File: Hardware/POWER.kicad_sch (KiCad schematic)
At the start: 57 parts, among them J4 Conn_01x02, U3 TLV62080DSGR, U4 RT7272BGSP, U5 TPS259260DRCR

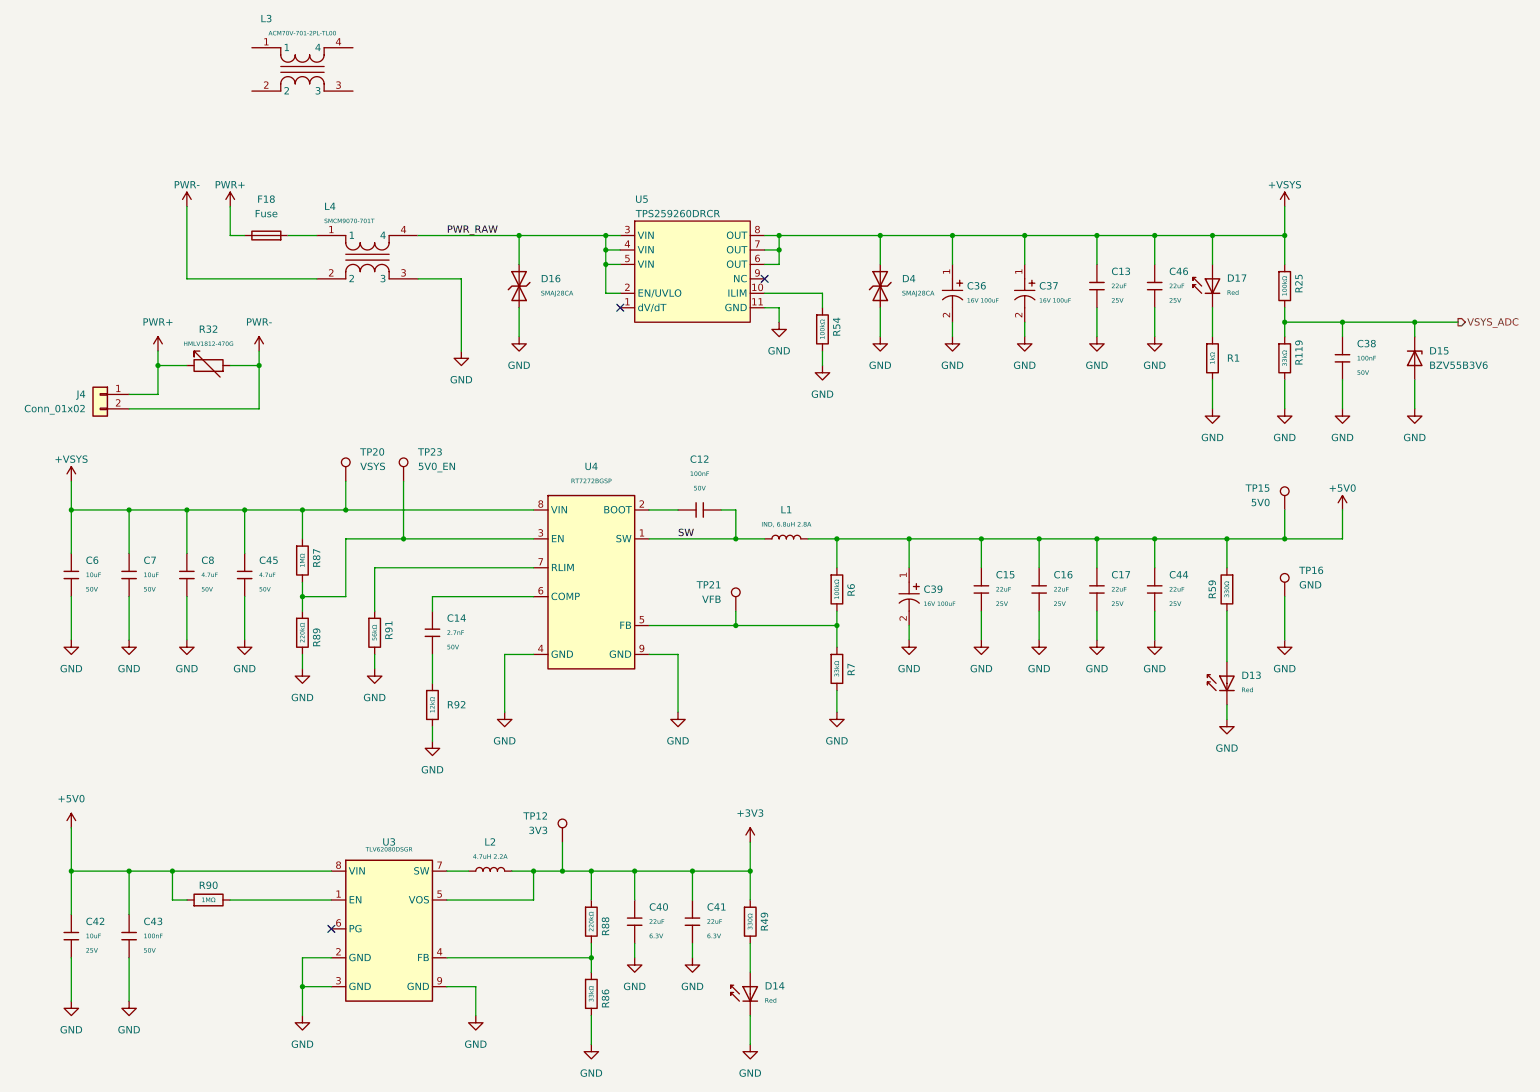
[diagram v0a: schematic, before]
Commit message: remove unused sheets
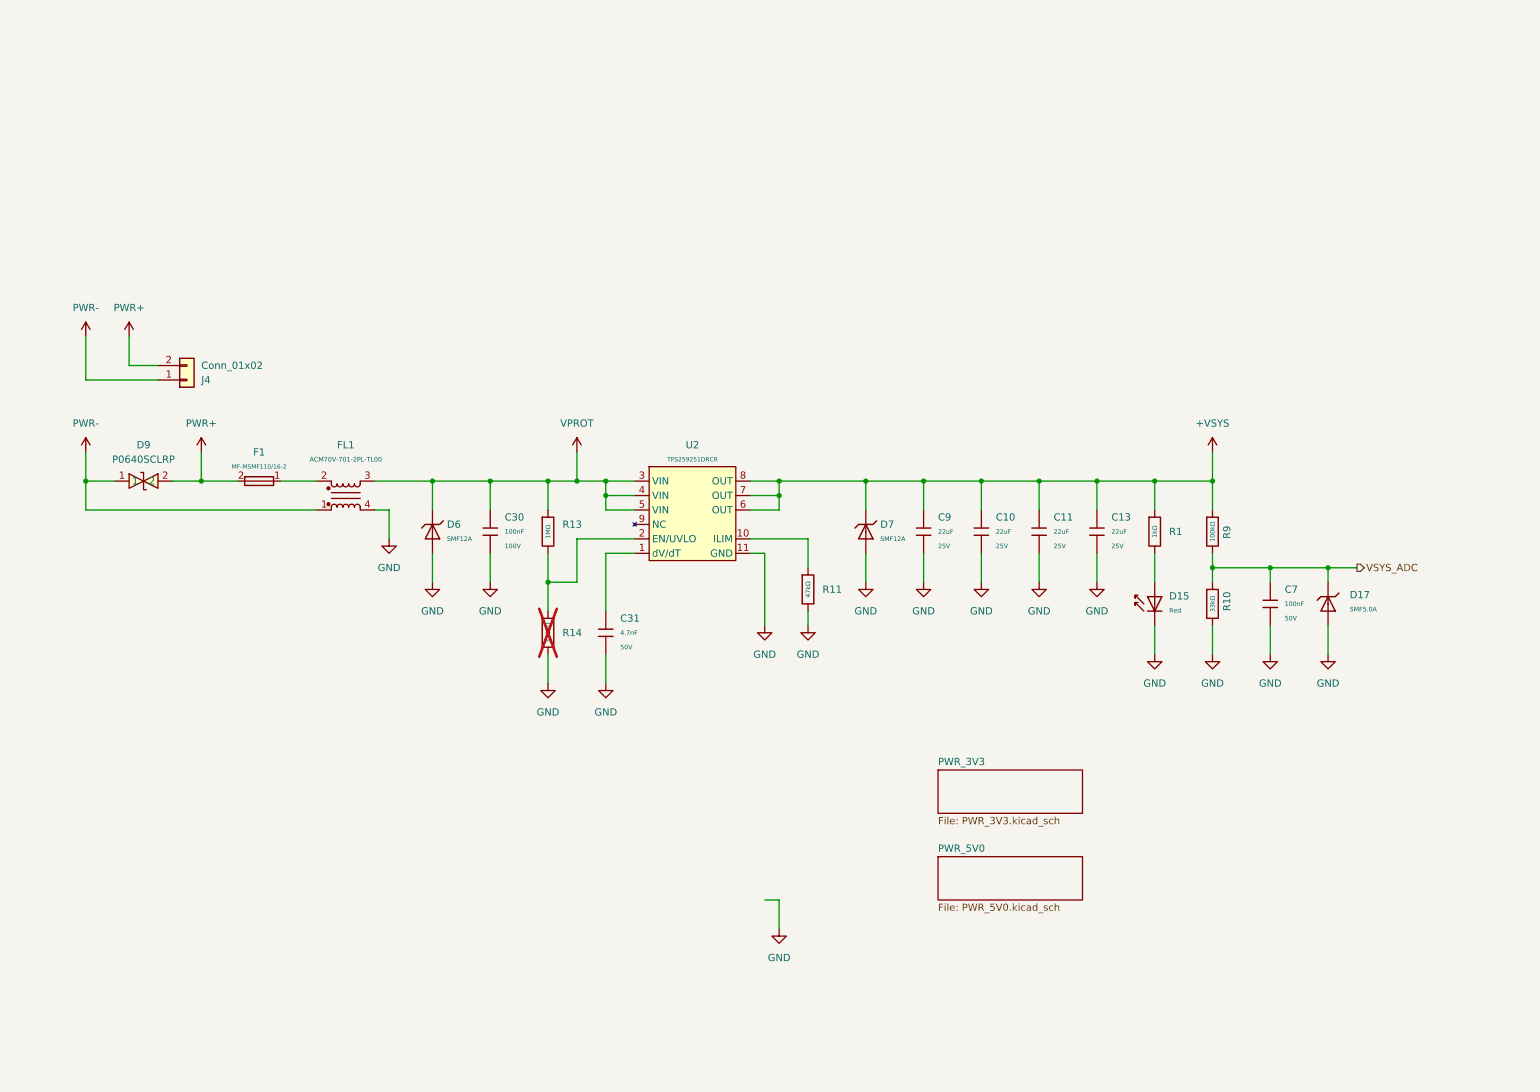
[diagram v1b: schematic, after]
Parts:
- removed C12, C38, C43: 100nF, PCM_JLCPCB:C_0603, symbol PCM_JLCPCB-Capacitors:0603,100nF
- removed C14: 2.7nF, PCM_JLCPCB:C_0603, symbol PCM_JLCPCB-Capacitors:0603,2.7nF
- removed C15, C16, C17, C44, C46: 22uF, PCM_JLCPCB:C_0805, symbol PCM_JLCPCB-Capacitors:0805,22uF
- removed C36, C37, C39: 16V 100uF, EasyEDA:CAP-SMD_BD6.3-L6.6-W6.6-LS7.2-FD, symbol EasyEDA:RVT100UF16V67RV0016
- removed C40, C41: 22uF, PCM_JLCPCB:C_0603, symbol PCM_JLCPCB-Capacitors:0603,22uF
- removed C42: 10uF, PCM_JLCPCB:C_0603, symbol PCM_JLCPCB-Capacitors:0603,10uF,(2)
- removed C45, C8: CL21A475KBQNNNE, PCM_JLCPCB:C_0805, symbol PCM_JLCPCB-Extended:CAP, 0805 4.7uF 50V
- removed C6, C7: 10uF, PCM_JLCPCB:C_0805, symbol PCM_JLCPCB-Capacitors:0805,10uF,(2)
- removed D13, D14, D17: Red, PCM_JLCPCB:D_0603, symbol PCM_JLCPCB-Diodes:LED,0603,Red
- removed D15: BZV55B3V6, Diode_SMD:D_MiniMELF, symbol Diode:BZV55B3V6
- removed D16, D4: SMAJ28CA, PCM_JLCPCB:D_SMA, symbol PCM_JLCPCB-Diodes:TVS-Bi,SMAJ28CA
- removed F18: Fuse, Resistor_SMD:R_1812_4532Metric_Pad1.30x3.40mm_HandSolder, symbol Device:Fuse
- removed L1: IND, 6.8uH 2.8A, PCM_JLCPCB:IND-SMD_L4.0-W4.0, symbol PCM_JLCPCB-Extended:IND, 6.8uH 2.8A
- removed L2: 4.7uH 2.2A, EASYEDA2KICAD:L1008, symbol PCM_JLCPCB-Extended:IND, 1uH 2A
- removed L3: ACM70V-701-2PL-TL00, EasyEDA:FILTER-SMD_4P-L7.0-W6.0-TL_ACM70V, symbol EasyEDA:ACM70V-701-2PL-TL00
- removed L4: SMCM9070-701T, EasyEDA:FILTER-SMD_4P-L9.0-W7.0-LS9.5-1, symbol EasyEDA:SMCM9070-701T
- removed R119, R7, R86: 33kΩ, PCM_JLCPCB:R_0603, symbol PCM_JLCPCB-Resistors:0603,33kΩ
- removed R25, R54, R6: 100kΩ, PCM_JLCPCB:R_0603, symbol PCM_JLCPCB-Resistors:0603,100kΩ
- removed R32: HMLV1812-470G, Resistor_SMD:R_1812_4532Metric_Pad1.30x3.40mm_HandSolder, symbol PCM_JLCPCB-Extended:MOV, HMLV1812-470G
- removed R49, R59: 330Ω, PCM_JLCPCB:R_0603, symbol PCM_JLCPCB-Resistors:0603,330Ω
- removed R87, R90: 1MΩ, PCM_JLCPCB:R_0603, symbol PCM_JLCPCB-Resistors:0603,1MΩ
- removed R88, R89: 220kΩ, PCM_JLCPCB:R_0603, symbol PCM_JLCPCB-Resistors:0603,220kΩ
- removed R91: 56kΩ, PCM_JLCPCB:R_0603, symbol PCM_JLCPCB-Resistors:0603,56kΩ
- removed R92: 12kΩ, PCM_JLCPCB:R_0603, symbol PCM_JLCPCB-Resistors:0603,12kΩ
- removed TP12: 3V3, TestPoint:TestPoint_Pad_D1.0mm, symbol Connector:TestPoint
- removed TP15: 5V0, TestPoint:TestPoint_Pad_D1.0mm, symbol Connector:TestPoint
- removed TP16: GND, TestPoint:TestPoint_Pad_D1.0mm, symbol Connector:TestPoint
- removed TP20: VSYS, TestPoint:TestPoint_Pad_D1.0mm, symbol Connector:TestPoint
- removed TP21: VFB, TestPoint:TestPoint_Pad_D1.0mm, symbol Connector:TestPoint
- removed TP23: 5V0_EN, TestPoint:TestPoint_Pad_D1.0mm, symbol Connector:TestPoint
- removed U3: TLV62080DSGR, Package_SON:WSON-8-1EP_2x2mm_P0.5mm_EP0.9x1.6mm, symbol PCM_JLCPCB-Extended:PMIC, TLV62080DSGR
- removed U4: RT7272BGSP, Package_SO:SOIC-8-1EP_3.9x4.9mm_P1.27mm_EP2.29x3mm, symbol AderbTech:PMIC, RT7272BGSP
- removed U5: TPS259260DRCR, EasyEDA:VSON-10_L3.0-W3.0-P0.50-TL-EP-1, symbol EasyEDA:TPS259260DRCR
- added C10, C11, C9: 22uF, PCM_JLCPCB:C_0805, symbol PCM_JLCPCB-Capacitors:0805,22uF
- added C30: 100nF, PCM_JLCPCB:C_0805, symbol PCM_JLCPCB-Capacitors:0805,100nF
- added C31: 4.7nF, PCM_JLCPCB:C_0603, symbol PCM_JLCPCB-Capacitors:0603,4.7nF
- added C7: 100nF, PCM_JLCPCB:C_0603, symbol PCM_JLCPCB-Capacitors:0603,100nF
- added D15: Red, PCM_JLCPCB:D_0603, symbol PCM_JLCPCB-Diodes:LED,0603,Red
- added D17: SMF5.0A, PCM_JLCPCB:D_SOD-123FL, symbol PCM_JLCPCB-Diodes:TVS-Uni,SMF5.0A
- added D6, D7: SMF12A, PCM_JLCPCB:D_SOD-123FL, symbol PCM_JLCPCB-Diodes:TVS-Uni,SMF12A
- added D9: P0640SCLRP, EasyEDA:SMB_L4.6-W3.6-LS5.3-BI, symbol EasyEDA:P0640SCLRP
- added F1: MF-MSMF110/16-2, Fuse:Fuse_1812_4532Metric_Pad1.30x3.40mm_HandSolder, symbol PCM_JLCPCB-Extended:Fuse, MF-MSMF110/16-2
- added FL1: ACM70V-701-2PL-TL00, EasyEDA:FILTER-SMD_4P-L7.0-W6.0-TL_ACM70V, symbol PCM_JLCPCB-Extended:CMC, ACM70V-701-2PL-TL00
- added R10: 33kΩ, PCM_JLCPCB:R_0603, symbol PCM_JLCPCB-Resistors:0603,33kΩ
- added R11: 47kΩ, PCM_JLCPCB:R_0603, symbol PCM_JLCPCB-Resistors:0603,47kΩ
- added R13: 1MΩ, PCM_JLCPCB:R_0603, symbol PCM_JLCPCB-Resistors:0603,1MΩ
- added R14: 330kΩ, PCM_JLCPCB:R_0603, symbol PCM_JLCPCB-Resistors:0603,330kΩ
- added R9: 100kΩ, PCM_JLCPCB:R_0603, symbol PCM_JLCPCB-Resistors:0603,100kΩ
- added U2: TPS259251DRCR, EasyEDA:WSON-10_L3.0-W3.0-P0.50-BL-EP, symbol EasyEDA:TPS259251DRCR
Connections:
- net +VSYS: now also R1.1, C10.1, C11.1, C9.1, D7.1, R9.1, U2.6 (OUT), U2.7 (OUT), U2.8 (OUT)
- net GND: now also C10.2, C11.2, C30.2, C31.2, C7.2, C9.2, D15.1, D17.2, D6.2, D7.2, FL1.4, R10.2, R11.2, R14.2, U2.11 (GND); no longer R1.2
- net PWR+: now also J4.2 (Pin_2), D9.2, F1.2; no longer J4.1 (Pin_1)
- net PWR-: now also J4.1 (Pin_1), D9.1, FL1.1; no longer J4.2 (Pin_2)
- net VSYS_ADC: now also C7.1, D17.1, R10.1, R9.2
- new net: F1.1, FL1.2
- new net: C31.1, U2.1 (dV/dT)
- new net: R11.1, U2.10 (ILIM)
- new net: R13.2, R14.1, U2.2 (EN/UVLO)
- new net: D15.2, R1.2
- new net VPROT: C30.1, D6.1, FL1.3, R13.1, U2.3 (VIN), U2.4 (VIN), U2.5 (VIN)
- no-connect marks 3 -> 0
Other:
- added sheet PWR_3V3 (PWR_3V3.kicad_sch)
- added sheet PWR_5V0 (PWR_5V0.kicad_sch)
- moved on the sheet: C13, J4, R1
